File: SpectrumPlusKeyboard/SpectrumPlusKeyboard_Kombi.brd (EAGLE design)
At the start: 254.5 x 99.2 mm, 109 parts, among them IC1 4066, IC2 4066, IC3 4066, IC4 4066, IC5 4066, SW1 TRUE VIDEO, SW10 8, SW11 9, SW12 0, SW13 BREAK, SW14 DELETE, SW15 GRAPH, SW16 Q, SW17 W, SW18 E, SW19 R, SW2 INVERSE VIDEO, SW20 T, SW21 Y, SW22 U, SW23 I, SW24 O, SW25 P, SW26 EXTEND MODE, SW27 EDIT, SW28 A, SW29 S, SW3 1, SW30 D, SW31 F, SW32 G, SW33 H, SW34 J, SW35 K, SW36 L, SW37 ENTER, SW38 CAPS SHIFT, SW39 CAPS LOCK, SW4 2, SW40 Z, SW41 X, SW42 C, SW43 V, SW44 B, SW45 N, SW46 M, SW47 ., SW48 CAPS SHIFT, SW49 SYMBOL SHIFT, SW5 3, SW50 ;, SW51 \', SW52 LEFT, SW53 RIGHT, SW54 SPACE, SW55 UP, SW56 DOWN, SW57 ,, SW58 SYMBOL SHIFT, SW6 4, SW7 5, SW8 6, SW9 7

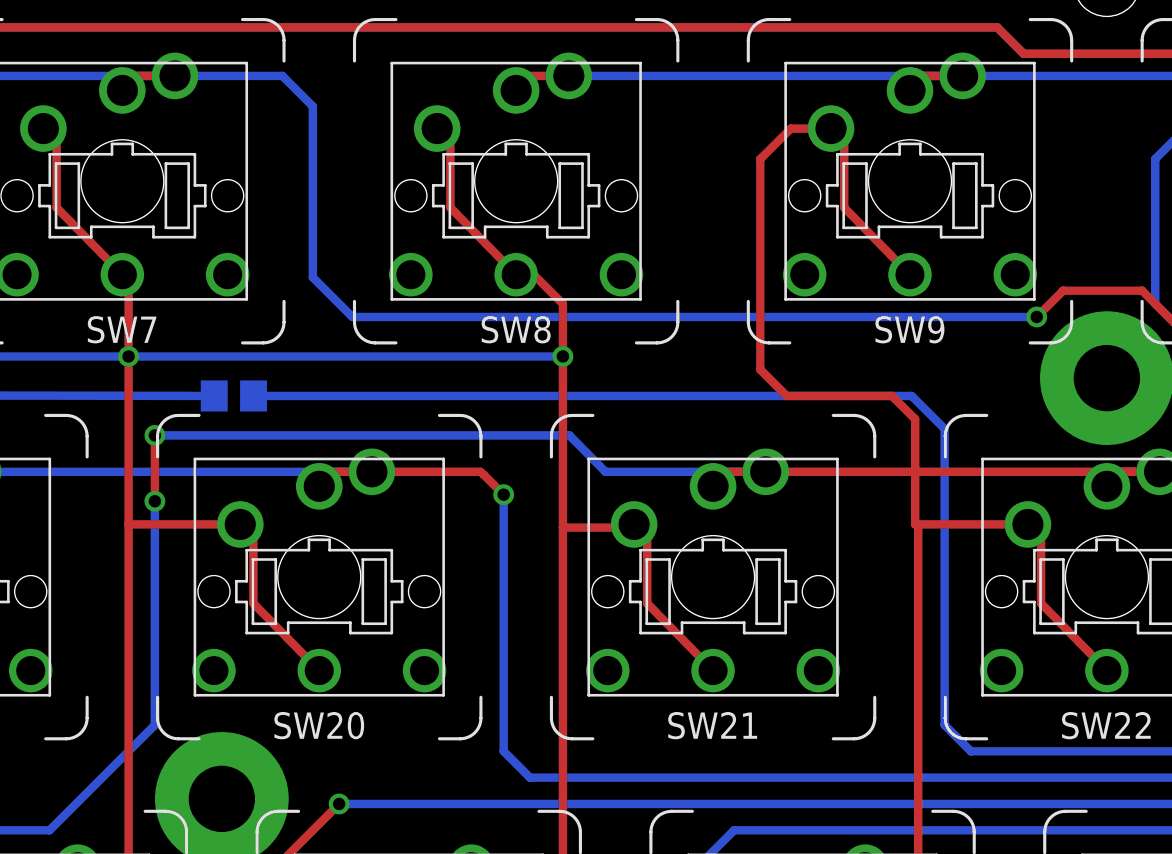
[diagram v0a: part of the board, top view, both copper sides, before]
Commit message: Corrected Error around SW9
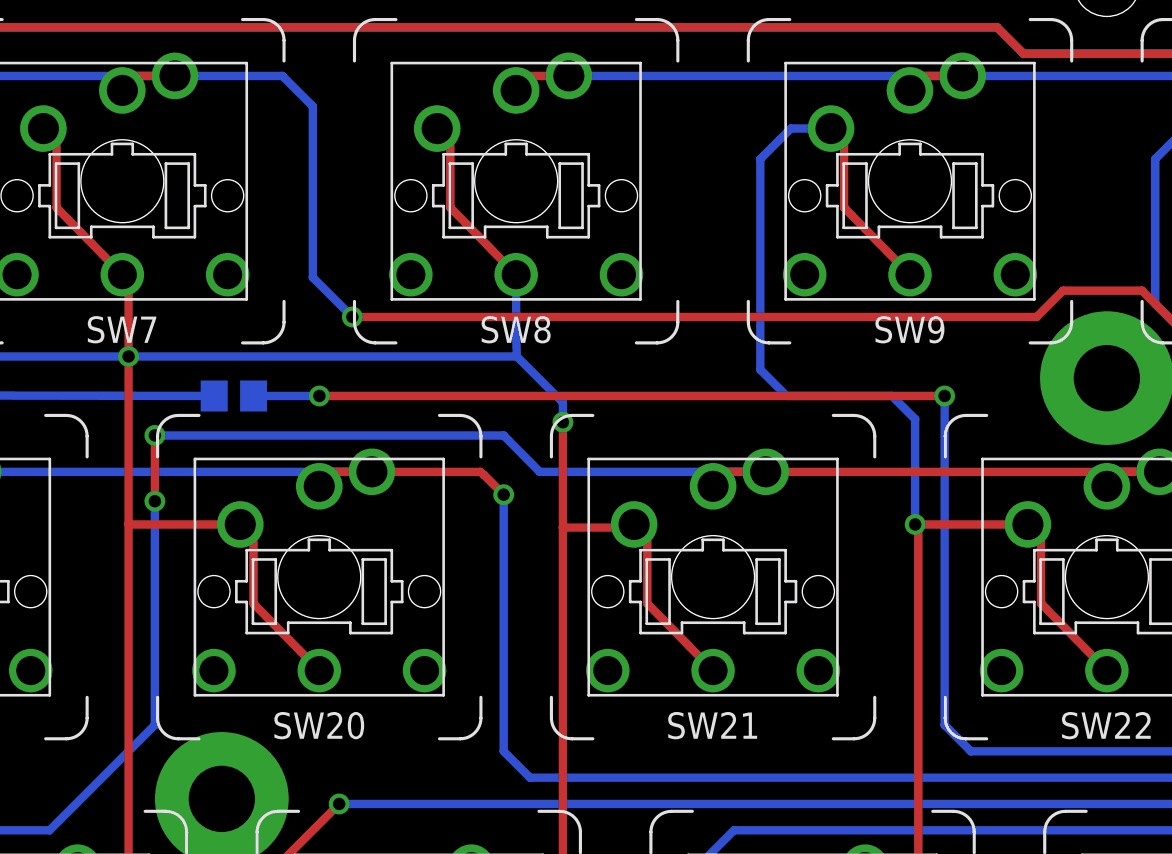
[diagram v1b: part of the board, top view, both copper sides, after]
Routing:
- net ROW1: track 273.5 -> 270.8 mm
- net GND: track 728.1 -> 729.1 mm, vias 21 -> 23
- net ROW2: vias 6 -> 7
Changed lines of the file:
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@@
 <via x="103.505" y="6.35" extent="1-16" drill="0.6"/>
 <wire x1="210.82" y1="66.675" x2="210.82" y2="62.38" width="0.4064" layer="16"/>
-<wire x1="145.04" y1="62.38" x2="137.31" y2="62.38" width="0.4064" layer="16"/>
-<wire x1="137.31" y1="62.38" x2="135.5725" y2="64.135" width="0.4064" layer="16"/>
-<wire x1="135.5725" y1="64.135" x2="115.57" y2="64.135" width="0.4064" layer="16"/>
+<wire x1="145.04" y1="62.38" x2="134.135" y2="62.38" width="0.4064" layer="16"/>
+<wire x1="134.135" y1="62.38" x2="132.3975" y2="64.135" width="0.4064" layer="16"/>
+<wire x1="132.3975" y1="64.135" x2="115.57" y2="64.135" width="0.4064" layer="16"/>
 <via x="115.57" y="64.135" extent="1-16" drill="0.6"/>
 <wire x1="115.57" y1="64.135" x2="115.57" y2="60.96" width="0.4064" layer="1"/>
@@
 <wire x1="114.3" y1="43.18" x2="114.3" y2="59.84" width="0.4064" layer="1"/>
 <wire x1="116.84" y1="22.86" x2="116.84" y2="40.74" width="0.4064" layer="1"/>
-<wire x1="135.255" y1="67.945" x2="135.255" y2="59.69" width="0.4064" layer="1"/>
+<wire x1="135.255" y1="64.77" x2="135.255" y2="59.69" width="0.4064" layer="1"/>
 <wire x1="135.255" y1="59.69" x2="138.54" y2="59.69" width="0.4064" layer="1"/>
 <wire x1="138.54" y1="59.69" x2="138.69" y2="59.84" width="0.4064" layer="1"/>
@@
 <via x="145.415" y="12.7" extent="1-16" drill="0.6"/>
 <via x="116.84" y="40.74" extent="1-16" drill="0.6"/>
-<via x="135.255" y="67.945" extent="1-16" drill="0.6"/>
+<via x="135.255" y="64.77" extent="1-16" drill="0.6"/>
 <contactref element="SW7" pad="1B"/>
 <contactref element="SW8" pad="1B"/>
@@
 <contactref element="SW43" pad="1B"/>
 <wire x1="79.375" y1="66.675" x2="71.12" y2="66.675" width="0.4064" layer="1"/>
-<wire x1="135.255" y1="67.945" x2="114.3" y2="67.945" width="0.4064" layer="16"/>
+<wire x1="135.255" y1="64.77" x2="135.255" y2="65.7225" width="0.4064" layer="16"/>
+<wire x1="135.255" y1="65.7225" x2="133.0325" y2="67.945" width="0.4064" layer="16"/>
+<wire x1="133.0325" y1="67.945" x2="114.3" y2="67.945" width="0.4064" layer="16"/>
 <via x="114.3" y="67.945" extent="1-16" drill="0.6"/>
-<wire x1="133" y1="71.89" x2="133.85" y2="71.89" width="0.4064" layer="1"/>
-<wire x1="133.85" y1="71.89" x2="135.255" y2="70.485" width="0.4064" layer="1"/>
-<wire x1="135.255" y1="70.485" x2="135.255" y2="67.945" width="0.4064" layer="1"/>
 <wire x1="114.3" y1="59.84" x2="114.3" y2="67.945" width="0.4064" layer="1"/>
 <wire x1="114.3" y1="67.945" x2="114.3" y2="71.59" width="0.4064" layer="1"/>
@@
 <wire x1="90.805" y1="73.66" x2="86.36" y2="73.66" width="0.4064" layer="16"/>
 <via x="86.36" y="73.66" extent="1-16" drill="0.6"/>
+<wire x1="133" y1="71.89" x2="133" y2="68.865" width="0.4064" layer="16"/>
+<wire x1="133" y1="68.865" x2="133.0325" y2="67.945" width="0.4064" layer="16"/>
 </signal>
 <signal name="ROW2">
@@
 <wire x1="93.98" y1="21.59" x2="95.84" y2="21.59" width="0.4064" layer="16"/>
 <wire x1="95.84" y1="21.59" x2="95.89" y2="21.64" width="0.4064" layer="16"/>
-<wire x1="148.19" y1="78.94" x2="146.25" y2="78.94" width="0.4064" layer="1"/>
-<wire x1="146.25" y1="78.94" x2="144.78" y2="77.47" width="0.4064" layer="1"/>
-<wire x1="144.78" y1="77.47" x2="144.78" y2="67.31" width="0.4064" layer="1"/>
-<wire x1="144.78" y1="67.31" x2="146.05" y2="66.04" width="0.4064" layer="1"/>
-<wire x1="146.05" y1="66.04" x2="151.13" y2="66.04" width="0.4064" layer="1"/>
-<wire x1="151.13" y1="66.04" x2="152.25" y2="64.92" width="0.4064" layer="1"/>
+<wire x1="148.19" y1="78.94" x2="146.25" y2="78.94" width="0.4064" layer="16"/>
+<wire x1="146.25" y1="78.94" x2="144.78" y2="77.47" width="0.4064" layer="16"/>
+<wire x1="144.78" y1="77.47" x2="144.78" y2="67.31" width="0.4064" layer="16"/>
+<wire x1="144.78" y1="67.31" x2="146.05" y2="66.04" width="0.4064" layer="16"/>
+<wire x1="146.05" y1="66.04" x2="151.13" y2="66.04" width="0.4064" layer="16"/>
+<wire x1="151.13" y1="66.04" x2="152.25" y2="64.92" width="0.4064" layer="16"/>
 <wire x1="157.69" y1="59.84" x2="152.4" y2="59.84" width="0.4064" layer="1"/>
 <wire x1="152.4" y1="59.84" x2="152.25" y2="59.84" width="0.4064" layer="1"/>
@@
 <via x="57.785" y="47.625" extent="1-16" drill="0.6"/>
 <wire x1="69.85" y1="64.135" x2="68.58" y2="65.405" width="0.4064" layer="16"/>
-<wire x1="152.25" y1="59.84" x2="152.25" y2="64.92" width="0.4064" layer="1"/>
+<wire x1="152.25" y1="59.84" x2="152.25" y2="64.92" width="0.4064" layer="16"/>
 <wire x1="20.955" y1="48.895" x2="38.735" y2="48.895" width="0.4064" layer="16"/>
 <wire x1="38.735" y1="48.895" x2="40.64" y2="50.8" width="0.4064" layer="16"/>
@@
 <wire x1="97.79" y1="59.69" x2="97.79" y2="69.1" width="0.4064" layer="1"/>
 <wire x1="97.79" y1="69.1" x2="95" y2="71.89" width="0.4064" layer="1"/>
+<via x="152.25" y="59.84" extent="1-16" drill="0.6"/>
 </signal>
 <signal name="ROW3">
@@
 <wire x1="184.15" y1="66.675" x2="181.76" y2="66.675" width="0.4064" layer="16"/>
 <wire x1="181.76" y1="66.675" x2="181.44" y2="66.355" width="0.4064" layer="16"/>
-<wire x1="125.095" y1="69.85" x2="158.115" y2="69.85" width="0.4064" layer="16"/>
+<wire x1="125.095" y1="69.85" x2="158.115" y2="69.85" width="0.4064" layer="1"/>
 <wire x1="158.115" y1="69.85" x2="159.385" y2="71.12" width="0.4064" layer="1"/>
 <wire x1="159.385" y1="71.12" x2="163.195" y2="71.12" width="0.4064" layer="1"/>
@@
 <contactref element="SW6" pad="2B"/>
 <contactref element="SW7" pad="2B"/>
-<via x="158.115" y="69.85" extent="1-16" drill="0.6"/>
+<via x="125.095" y="69.85" extent="1-16" drill="0.6"/>
 </signal>
 <signal name="SW5">
@@
 <via x="5.08" y="46.355" extent="1-16" drill="0.6"/>
 <wire x1="5.08" y1="46.355" x2="12.7" y2="46.355" width="0.4064" layer="1"/>
-<wire x1="120.33" y1="66.04" x2="152.0825" y2="66.04" width="0.4064" layer="16"/>
+<wire x1="120.33" y1="66.04" x2="123.5075" y2="66.04" width="0.4064" layer="16"/>
 <wire x1="-3.175" y1="46.355" x2="5.08" y2="46.355" width="0.4064" layer="1"/>
 <wire x1="154.94" y1="48.895" x2="153.67" y2="50.165" width="0.4064" layer="16"/>
-<wire x1="153.67" y1="50.165" x2="153.67" y2="64.4525" width="0.4064" layer="16"/>
-<wire x1="153.67" y1="64.4525" x2="152.0825" y2="66.04" width="0.4064" layer="16"/>
+<wire x1="153.67" y1="50.165" x2="153.67" y2="66.04" width="0.4064" layer="16"/>
+<wire x1="153.67" y1="66.04" x2="123.5075" y2="66.04" width="0.4064" layer="1"/>
 <wire x1="225.425" y1="50.165" x2="226.06" y2="50.8" width="0.4064" layer="16"/>
 <wire x1="226.06" y1="50.8" x2="226.06" y2="63.67" width="0.4064" layer="16"/>
@@
 <wire x1="29.835" y1="69.285" x2="29.845" y2="69.285" width="0.4064" layer="16"/>
 <wire x1="29.845" y1="69.285" x2="29.845" y2="66.675" width="0.4064" layer="16"/>
+<via x="153.67" y="66.04" extent="1-16" drill="0.6"/>
+<via x="123.5075" y="66.04" extent="1-16" drill="0.6"/>
 </signal>
 <signal name="N$1">
